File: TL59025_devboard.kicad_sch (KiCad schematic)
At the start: 67 parts, among them J1 UPDI, J2 USB_C_Receptacle_USB2.0, J3 Cascade In, J4 Cascade Out, SW1 SW_Push, U1 AMS1117-3.3, U2 ATtiny414-SS, U3 CH340E, U4 TL59025, U5 TL59025

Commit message: Add IBOM and render images
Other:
- company: (none) -> Sleepy Pony Labs
- title: (none) -> TL59025 Devboard
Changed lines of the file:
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@@
 (kicad_sch (version 20211123) (generator eeschema)
   (paper "A4")
+  (title_block
+    (title "TL59025 Devboard")
+    (date "2022-09-18")
+    (rev "1")
+    (company "Sleepy Pony Labs")
+  )
   (junction (at 265.43 137.16) (diameter 0) (color 0 0 0 0)
   )

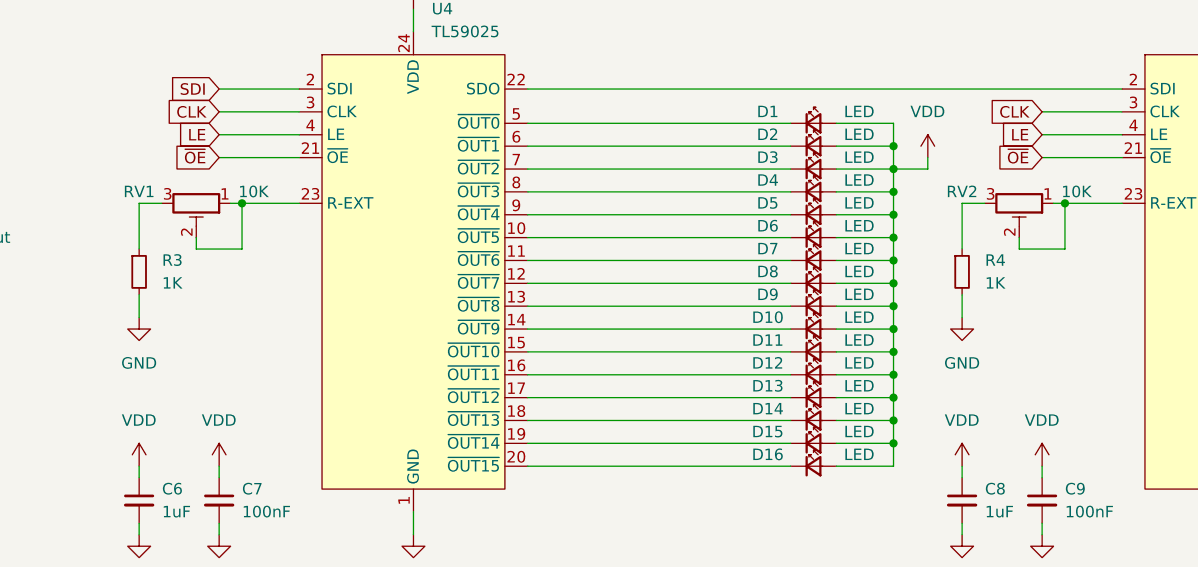
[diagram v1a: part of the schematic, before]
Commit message: Change R3 and R4 to 510R for maximum current range
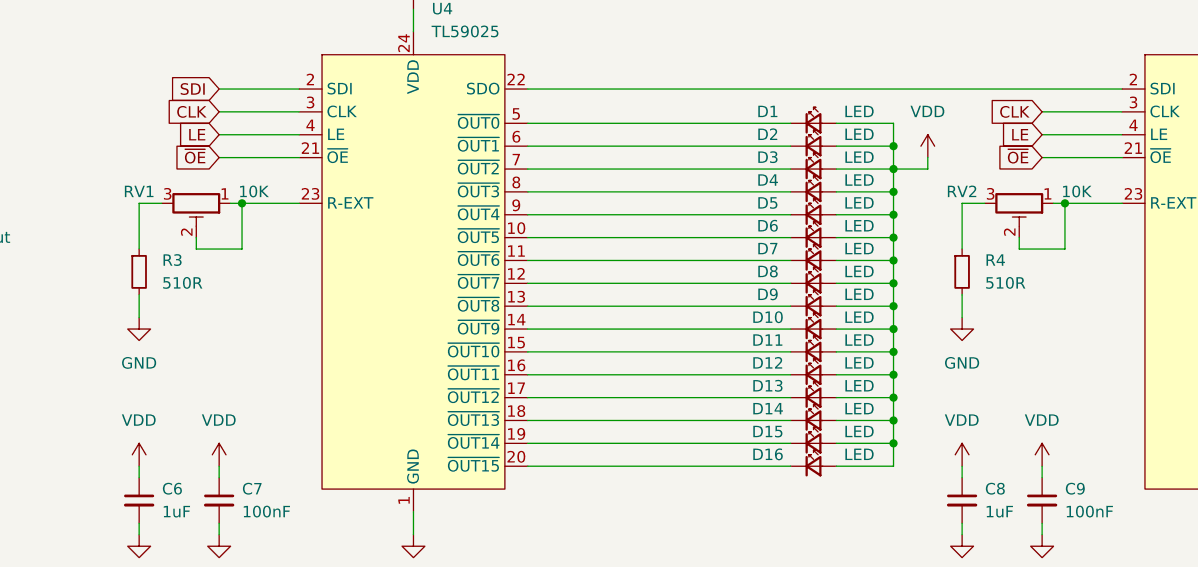
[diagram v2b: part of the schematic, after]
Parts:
- R3, R4: value 1K -> 510R
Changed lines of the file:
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@@
       (effects (font (size 1.27 1.27)) (justify left))
     )
-    (property "Value" "1K" (id 1) (at 184.15 129.5399 0)
+    (property "Value" "510R" (id 1) (at 184.15 129.5399 0)
       (effects (font (size 1.27 1.27)) (justify left))
     )
@@
       (effects (font (size 1.27 1.27)) (justify left))
     )
-    (property "Value" "1K" (id 1) (at 92.71 129.5399 0)
+    (property "Value" "510R" (id 1) (at 92.71 129.5399 0)
       (effects (font (size 1.27 1.27)) (justify left))
     )
@@
     )
     (path "/536c8a1e-4b0f-4e5b-aaa5-f878d17b639c"
-      (reference "R3") (unit 1) (value "1K") (footprint "Resistor_SMD:R_0603_1608Metric")
+      (reference "R3") (unit 1) (value "510R") (footprint "Resistor_SMD:R_0603_1608Metric")
     )
     (path "/3f4aaa17-2969-4cd0-8d5b-5abf785dc346"
-      (reference "R4") (unit 1) (value "1K") (footprint "Resistor_SMD:R_0603_1608Metric")
+      (reference "R4") (unit 1) (value "510R") (footprint "Resistor_SMD:R_0603_1608Metric")
     )
     (path "/bee6e674-5259-4f60-b419-61493fd54f35"
